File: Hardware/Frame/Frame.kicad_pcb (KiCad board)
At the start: 2 copper layers, 80.2 x 12.2 mm, 10 parts, among them J3 Screw_Terminal_01x02, J4 USB_C_Receptacle_PowerOnly_6P, U1 AMS1117-1.8

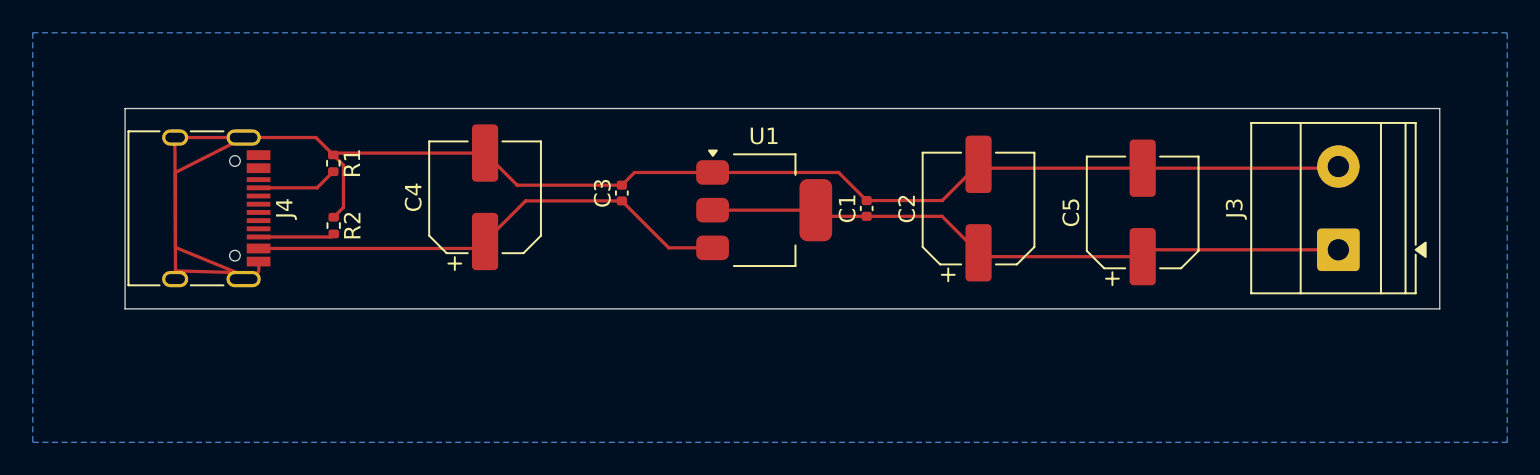
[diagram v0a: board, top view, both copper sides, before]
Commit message: added glasses functionality.
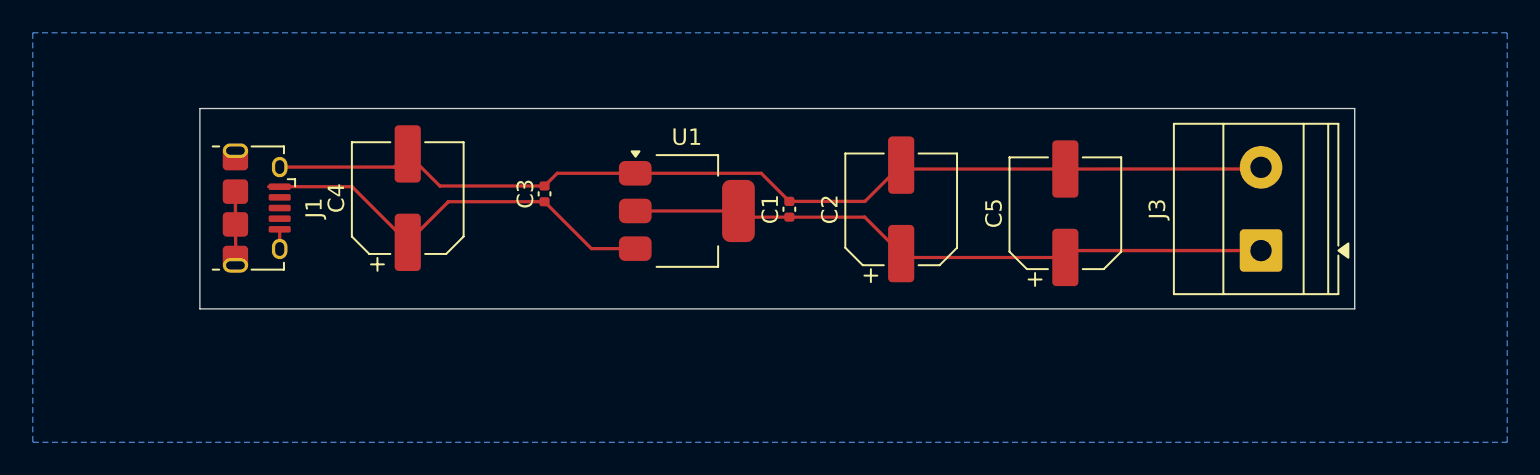
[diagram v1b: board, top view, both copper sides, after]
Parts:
- removed J4: USB_C_Receptacle_PowerOnly_6P, Connector_USB:USB_C_Receptacle_HRO_TYPE-C-31-M-12
- removed R1, R2: 5.1k, Resistor_SMD:R_0402_1005Metric
- added J1: USB_B_Micro, Connector_USB:USB_Micro-B_Amphenol_10118194_Horizontal, F.Cu at (108.7, 105.7)
- moved C2 4.72 mm to (148.0, 105.8)
- moved C1 4.72 mm to (141.2, 105.8)
- moved C4 4.72 mm to (117.9, 105.1)
- moved C5 4.72 mm to (158.0, 106.0)
- moved J3 4.72 mm to (170.0, 108.3)
- moved U1 4.72 mm to (134.9, 105.9)
- moved C3 4.72 mm to (126.2, 104.8)
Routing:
- net GND: track 67.8 -> 54.3 mm
- net Net-(J4-CC1): track 4.97 -> 0.00 mm
- net Net-(J4-CC2): track 4.66 -> 0.00 mm
- net +5VD: track 29.1 -> 26.0 mm
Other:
- board size 80.2 x 12.2 mm -> 70.5 x 12.2 mm
